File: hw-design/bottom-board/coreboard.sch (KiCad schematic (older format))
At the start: 12 parts, among them J7 Conn_02x50_Odd_Even, J8 Conn_02x50_Odd_Even, SW1 SW_PUSH, U4 AT24CS08-STUM

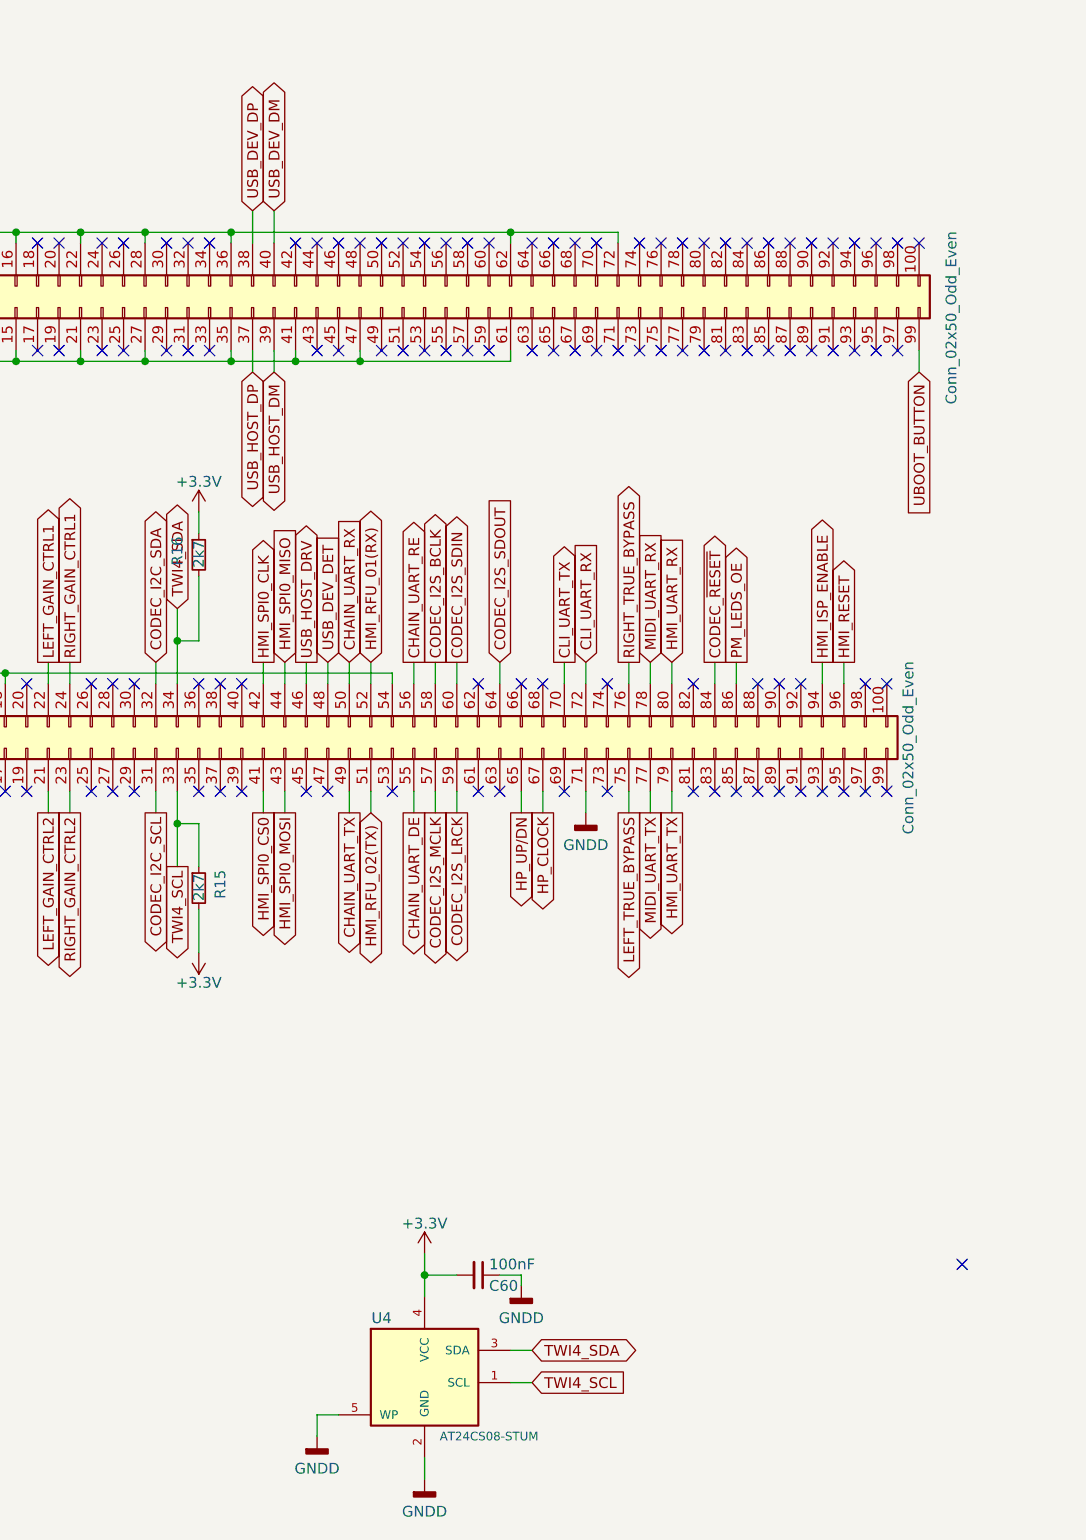
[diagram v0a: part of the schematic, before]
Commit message: changed a bottomboard to a minimal HMI testing unit
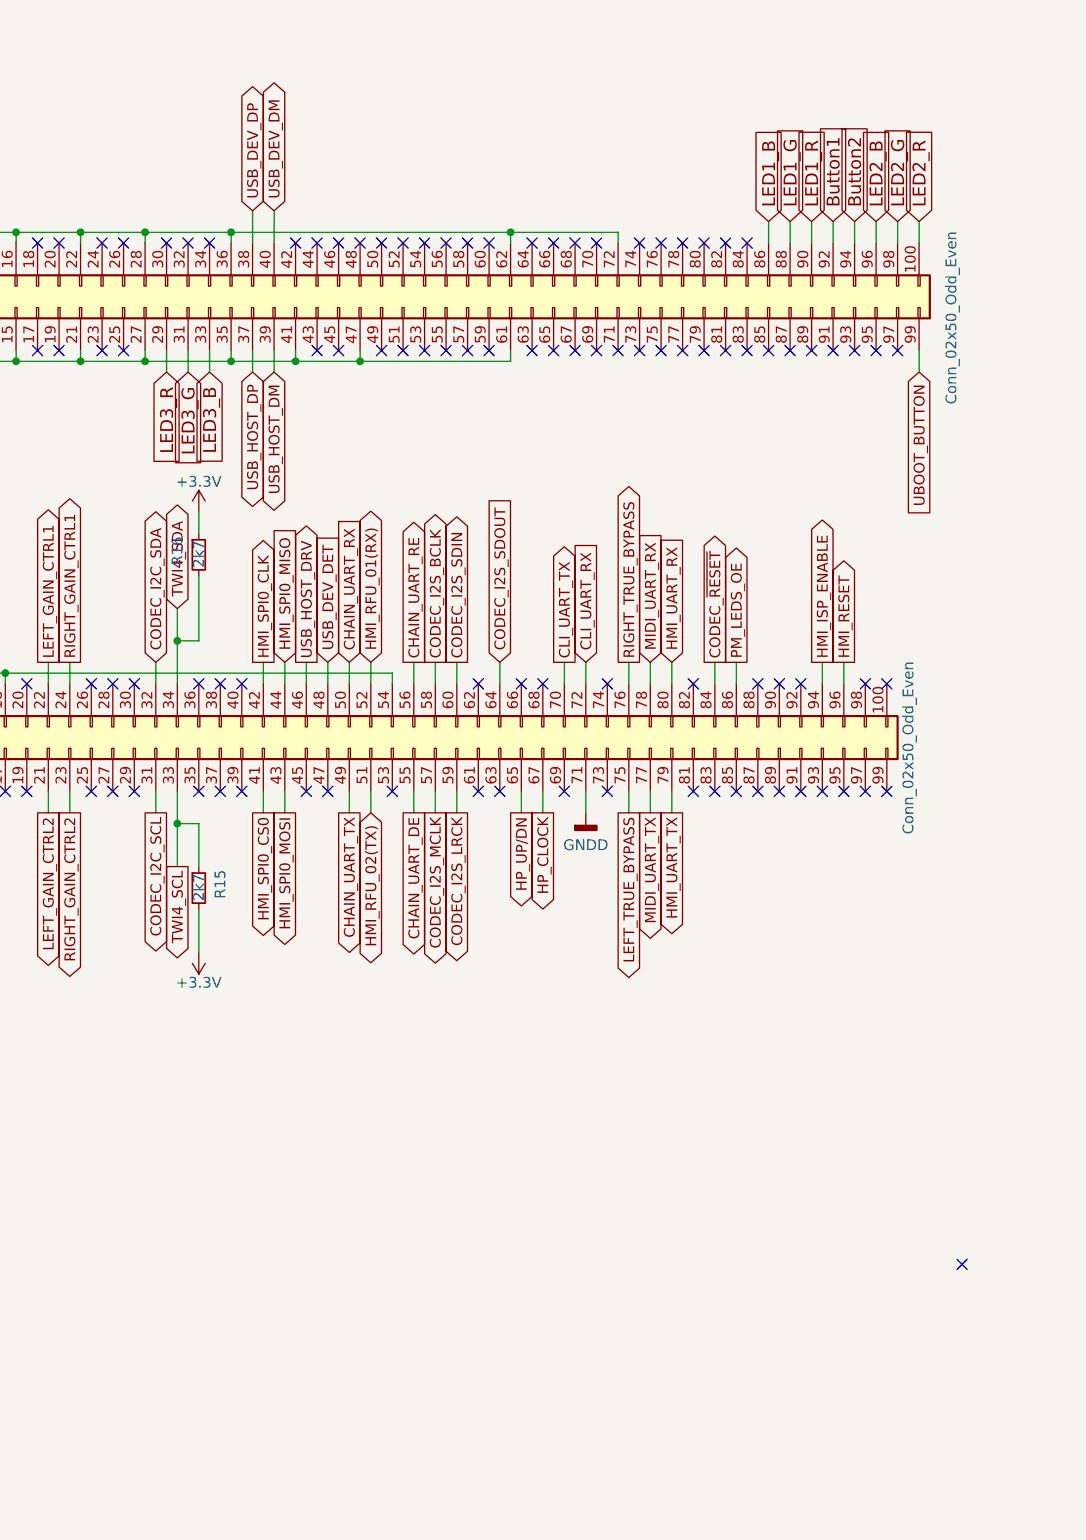
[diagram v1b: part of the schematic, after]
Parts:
- removed C60: 100nF, Capacitors_SMD:C_0603, symbol bottom-board-rescue:C_Small
- removed U4: AT24CS08-STUM, Package_TO_SOT_SMD:SOT-23-5, symbol bottom-board-rescue:AT24CS08-STUM
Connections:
- net LED2_R: now reaches J7.100 (Pin_100)
- net LED3_R: now reaches J7.29 (Pin_29)
- net LED3_G: now reaches J7.31 (Pin_31)
- net LED3_B: now reaches J7.33 (Pin_33)
- net LED1_B: now reaches J7.86 (Pin_86)
- net LED1_G: now reaches J7.88 (Pin_88)
- net LED1_R: now reaches J7.90 (Pin_90)
- net Button1: now reaches J7.92 (Pin_92)
- net Button2: now reaches J7.94 (Pin_94)
- net LED2_B: now reaches J7.96 (Pin_96)
- net LED2_G: now reaches J7.98 (Pin_98)
- no-connect marks 130 -> 119
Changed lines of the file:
@@
 EESchema Schematic File Version 4
 LIBS:bottom-board-cache
-EELAYER 26 0
+EELAYER 29 0
 EELAYER END
 $Descr A4 11693 8268
 encoding utf-8
-Sheet 4 12
-Title "MOD Duo - Bottom Board"
+Sheet 3 7
+Title "MOD Duo -HMI testing board"
 Date ""
-Rev ""
-Comp "MOD"
-Comment1 ""
-Comment2 ""
-Comment3 ""
-Comment4 ""
+Rev "1.0"
+Comp "MOD Devices GmbH"
+Comment1 "Controller board Tester"
+Comment2 "used for the MOD Duo"
+Comment3 "or MOD Duo X controller"
+Comment4 "Compatible w/ Marsboard SoM"
 $EndDescr
 $Comp
@@
 	-1   0    0    1
 $EndComp
-Text GLabel 6100 6700 2    50   BiDi ~ 0
-TWI4_SDA
-Text GLabel 6100 6850 2    50   Input ~ 0
-TWI4_SCL
-$Comp
-L bottom-board-rescue:GNDD-power #PWR059
-U 1 1 55FAFACA
-P 5600 7300
-F 0 "#PWR059" H 5600 7050 50  0001 C CNN
-F 1 "GNDD" H 5600 7150 50  0000 C CNN
-F 2 "" H 5600 7300 60  0000 C CNN
-F 3 "" H 5600 7300 60  0000 C CNN
-	1    5600 7300
-	1    0    0    -1
-$EndComp
-Wire Wire Line
-	5600 7200 5600 7300
-$Comp
-L bottom-board-rescue:+3.3V-power #PWR060
-U 1 1 55FAFDCC
-P 5600 6250
-F 0 "#PWR060" H 5600 6100 50  0001 C CNN
-F 1 "+3.3V" H 5600 6390 50  0000 C CNN
-F 2 "" H 5600 6250 60  0000 C CNN
-F 3 "" H 5600 6250 60  0000 C CNN
-	1    5600 6250
-	1    0    0    -1
-$EndComp
 $Comp
 L bottom-board-rescue:R_Small R16
@@
 Wire Wire Line
 	1650 6450 1750 6450
-$Comp
-L bottom-board-rescue:C_Small C60
-U 1 1 567B7F33
-P 5850 6350
-F 0 "C60" V 5900 6400 50  0000 L CNN
-F 1 "100nF" V 5800 6400 50  0000 L CNN
-F 2 "Capacitors_SMD:C_0603" H 5850 6350 60  0001 C CNN
-F 3 "" H 5850 6350 60  0000 C CNN
-F 4 "C1608X7R1E104K080AA" H -5050 4250 50  0001 C CNN "MPN"
-	1    5850 6350
-	0    1    1    0
-$EndComp
-$Comp
-L bottom-board-rescue:GNDD-power #PWR063
-U 1 1 567B8370
-P 6050 6400
-F 0 "#PWR063" H 6050 6150 50  0001 C CNN
-F 1 "GNDD" H 6050 6250 50  0000 C CNN
-F 2 "" H 6050 6400 60  0000 C CNN
-F 3 "" H 6050 6400 60  0000 C CNN
-	1    6050 6400
-	1    0    0    -1
-$EndComp
-Wire Wire Line
-	5950 6350 6050 6350
-Wire Wire Line
-	6050 6350 6050 6400
-Connection ~ 5600 6350
-$Comp
-L bottom-board-rescue:AT24CS08-STUM U4
-U 1 1 568DDEB6
-P 5600 6800
-AR Path="/568DDEB6" Ref="U4"  Part="1"
-AR Path="/54F725AE/568DDEB6" Ref="U4"  Part="1"
-F 0 "U4" H 5400 7050 50  0000 C CNN
-F 1 "AT24CS08-STUM" H 5900 6500 40  0000 C CNN
-F 2 "Package_TO_SOT_SMD:SOT-23-5" H 5600 6800 35  0001 C CIN
-F 3 "" H 5600 6800 60  0000 C CNN
-F 4 "AT24CS08-STUM" H 5600 6800 60  0001 C CNN "MPN"
-	1    5600 6800
-	1    0    0    -1
-$EndComp
-Wire Wire Line
-	6100 6700 6000 6700
-Wire Wire Line
-	6000 6850 6100 6850
-$Comp
-L bottom-board-rescue:GNDD-power #PWR064
-U 1 1 568DE570
-P 5100 7100
-F 0 "#PWR064" H 5100 6850 50  0001 C CNN
-F 1 "GNDD" H 5100 6950 50  0000 C CNN
-F 2 "" H 5100 7100 60  0000 C CNN
-F 3 "" H 5100 7100 60  0000 C CNN
-	1    5100 7100
-	1    0    0    -1
-$EndComp
-Wire Wire Line
-	5200 7000 5100 7000
-Wire Wire Line
-	5100 7000 5100 7100
 Wire Wire Line
 	1750 6450 1750 6550
@@
 Wire Wire Line
 	2900 750  2800 750
-Wire Wire Line
-	5600 6350 5600 6250
 $Comp
 L bottom-board-rescue:Conn_02x50_Odd_Even-header J7
@@
 Text GLabel 3550 3500 1    50   Input ~ 0
 POWER_BUTTON
-Wire Wire Line
-	5600 6350 5750 6350
 Wire Wire Line
 	3000 1550 3000 1450
@@
 NoConn ~ 7000 1550
 NoConn ~ 7100 1550
-NoConn ~ 7200 1550
-NoConn ~ 7300 1550
-NoConn ~ 7400 1550
-NoConn ~ 7500 1550
-NoConn ~ 7600 1550
-NoConn ~ 7700 1550
-NoConn ~ 7800 1550
-NoConn ~ 7900 1550
 Wire Wire Line
 	7900 2150 7900 2050
@@
 Wire Wire Line
 	5300 2100 5000 2100
-NoConn ~ 4600 2050
-NoConn ~ 4500 2050
-NoConn ~ 4400 2050
 NoConn ~ 4200 2050
 NoConn ~ 4100 2050
@@
 Wire Wire Line
 	4450 4250 4450 4450
-Wire Wire Line
-	5600 6350 5600 6450
 Wire Wire Line
 	3950 4200 3950 4100
@@
 Wire Wire Line
 	4800 2150 4800 2050
+Text GLabel 7200 1450 1    60   Input ~ 0
+LED1_B
+Text GLabel 7300 1450 1    60   Input ~ 0
+LED1_G
+Text GLabel 7400 1450 1    60   Input ~ 0
+LED1_R
+Text GLabel 7700 1450 1    60   Input ~ 0
+LED2_B
+Text GLabel 7800 1450 1    60   Input ~ 0
+LED2_G
+Text GLabel 7900 1450 1    60   Input ~ 0
+LED2_R
+Text GLabel 4600 2150 3    60   Input ~ 0
+LED3_B
+Text GLabel 4500 2150 3    60   Input ~ 0
+LED3_G
+Text GLabel 4400 2150 3    60   Input ~ 0
+LED3_R
+Wire Wire Line
+	4600 2150 4600 2050
+Wire Wire Line
+	4500 2150 4500 2050
+Wire Wire Line
+	4400 2150 4400 2050
+Text GLabel 7500 1450 1    60   Input ~ 0
+Button1
+Text GLabel 7600 1450 1    60   Input ~ 0
+Button2
+Wire Wire Line
+	7200 1550 7200 1450
+Wire Wire Line
+	7300 1550 7300 1450
+Wire Wire Line
+	7400 1550 7400 1450
+Wire Wire Line
+	7500 1550 7500 1450
+Wire Wire Line
+	7600 1550 7600 1450
+Wire Wire Line
+	7700 1550 7700 1450
+Wire Wire Line
+	7800 1550 7800 1450
+Wire Wire Line
+	7900 1550 7900 1450
 $EndSCHEMATC

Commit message: added final BOM files
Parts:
- C30, C58: footprint Capacitors_SMD:C_0805 -> Capacitor_SMD:C_0805_2012Metric
- C31, C59: footprint Capacitors_SMD:C_0603 -> Capacitor_SMD:C_0603_1608Metric
- R14: footprint Resistors_SMD:R_0603 -> Resistor_SMD:R_0603_1608Metric
- renumbered J7 to P2, J8 to P3
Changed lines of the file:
@@
 F 0 "C31" V 2250 4200 50  0000 L CNN
 F 1 "100nF" V 2150 4200 50  0000 L CNN
-F 2 "Capacitors_SMD:C_0603" H 2200 4150 60  0001 C CNN
+F 2 "Capacitor_SMD:C_0603_1608Metric" H 2200 4150 60  0001 C CNN
 F 3 "" H 2200 4150 60  0000 C CNN
 F 4 "C1608X7R1E104K080AA" H -8700 2050 50  0001 C CNN "MPN"
@@
 F 0 "R14" H 1800 6250 50  0000 L CNN
 F 1 "10k" H 1800 6150 50  0000 L CNN
-F 2 "Resistors_SMD:R_0603" H 1750 6200 60  0001 C CNN
+F 2 "Resistor_SMD:R_0603_1608Metric" H 1750 6200 60  0001 C CNN
 F 3 "" H 1750 6200 60  0000 C CNN
 F 4 "RMCF0603JT10K0" H 0   -450 50  0001 C CNN "MPN"
@@
 F 0 "C30" V 2250 4000 50  0000 L CNN
 F 1 "10uF" V 2150 4000 50  0000 L CNN
-F 2 "Capacitors_SMD:C_0805" H 2200 3950 60  0001 C CNN
+F 2 "Capacitor_SMD:C_0805_2012Metric" H 2200 3950 60  0001 C CNN
 F 3 "" H 2200 3950 60  0000 C CNN
 F 4 "GRM219R61E106KA12D" H -3100 -1400 50  0001 C CNN "MPN"
@@
 F 0 "C59" V 2850 950 50  0000 L CNN
 F 1 "100nF" V 2750 950 50  0000 L CNN
-F 2 "Capacitors_SMD:C_0603" H 2800 900 60  0001 C CNN
+F 2 "Capacitor_SMD:C_0603_1608Metric" H 2800 900 60  0001 C CNN
 F 3 "" H 2800 900 60  0000 C CNN
 F 4 "C1608X7R1E104K080AA" H -8100 -1200 50  0001 C CNN "MPN"
@@
 F 0 "C58" V 3050 950 50  0000 L CNN
 F 1 "10uF" V 2950 950 50  0000 L CNN
-F 2 "Capacitors_SMD:C_0805" H 3000 900 60  0001 C CNN
+F 2 "Capacitor_SMD:C_0805_2012Metric" H 3000 900 60  0001 C CNN
 F 3 "" H 3000 900 60  0000 C CNN
 F 4 "GRM219R61E106KA12D" H -2300 -4450 50  0001 C CNN "MPN"
@@
 	2900 750  2800 750
 $Comp
-L bottom-board-rescue:Conn_02x50_Odd_Even-header J7
+L bottom-board-rescue:Conn_02x50_Odd_Even-header P2
 U 1 1 5C60E9FC
 P 5400 1800
-F 0 "J7" V 5446 4279 50  0000 L CNN
+F 0 "P2" V 5446 4279 50  0000 L CNN
 F 1 "Conn_02x50_Odd_Even" H 4900 -850 50  0000 L CNN
 F 2 "footprints-local:Pin_Header_Straight_2x50_Pitch1.27mm_SMD" H 5350 2300 50  0001 C CNN
 F 3 "~" H 5350 2300 50  0001 C CNN
+F 4 "" V 5400 1800 50  0001 C CNN "MPN"
 	1    5400 1800
 	0    -1   -1   0
 $EndComp
 $Comp
-L bottom-board-rescue:Conn_02x50_Odd_Even-header J8
+L bottom-board-rescue:Conn_02x50_Odd_Even-header P3
 U 1 1 5C60EAB7
 P 5250 3850
-F 0 "J8" V 5296 6329 50  0000 L CNN
+F 0 "P3" V 5296 6329 50  0000 L CNN
 F 1 "Conn_02x50_Odd_Even" H 4800 1250 50  0000 L CNN
 F 2 "footprints-local:Pin_Header_Straight_2x50_Pitch1.27mm_SMD" H 5200 4350 50  0001 C CNN
 F 3 "~" H 5200 4350 50  0001 C CNN
+F 4 "" V 5250 3850 50  0001 C CNN "MPN"
 	1    5250 3850
 	0    -1   -1   0
